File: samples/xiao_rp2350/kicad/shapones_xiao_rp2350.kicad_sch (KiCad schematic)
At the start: 61 parts, among them Q1 PMOS, Q2 NPN, Q3 NPN, SW1 POWER, SW10 MENU, SW2 A, SW3 B, SW4 SELECT, SW5 START, SW6 UP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

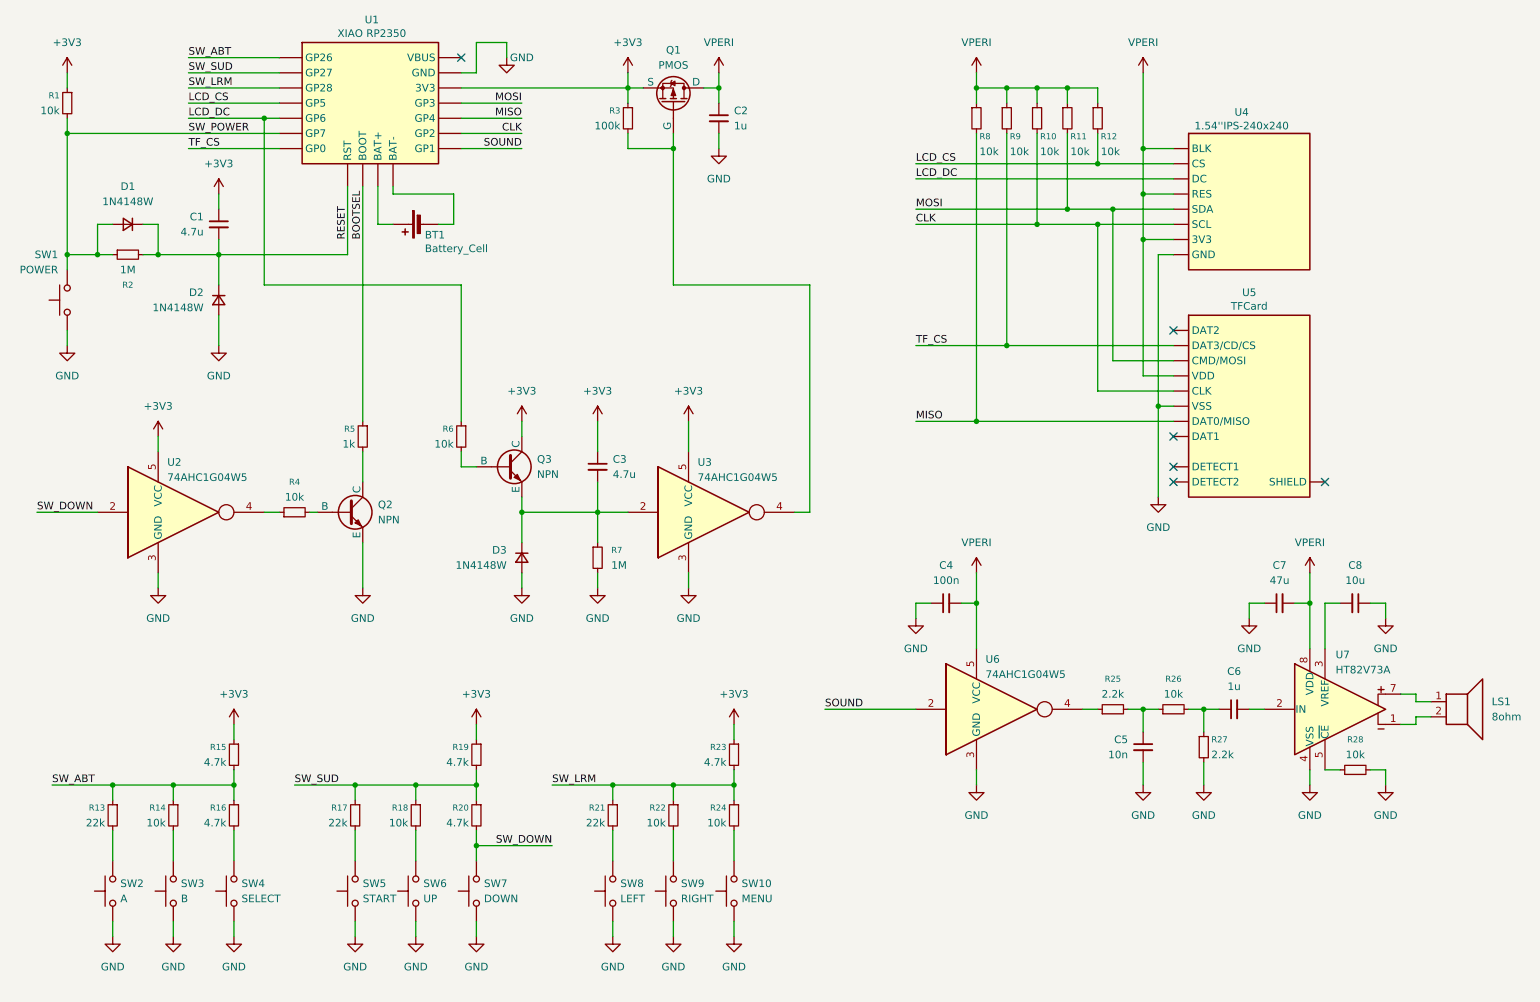
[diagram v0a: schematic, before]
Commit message: add deep sleep function
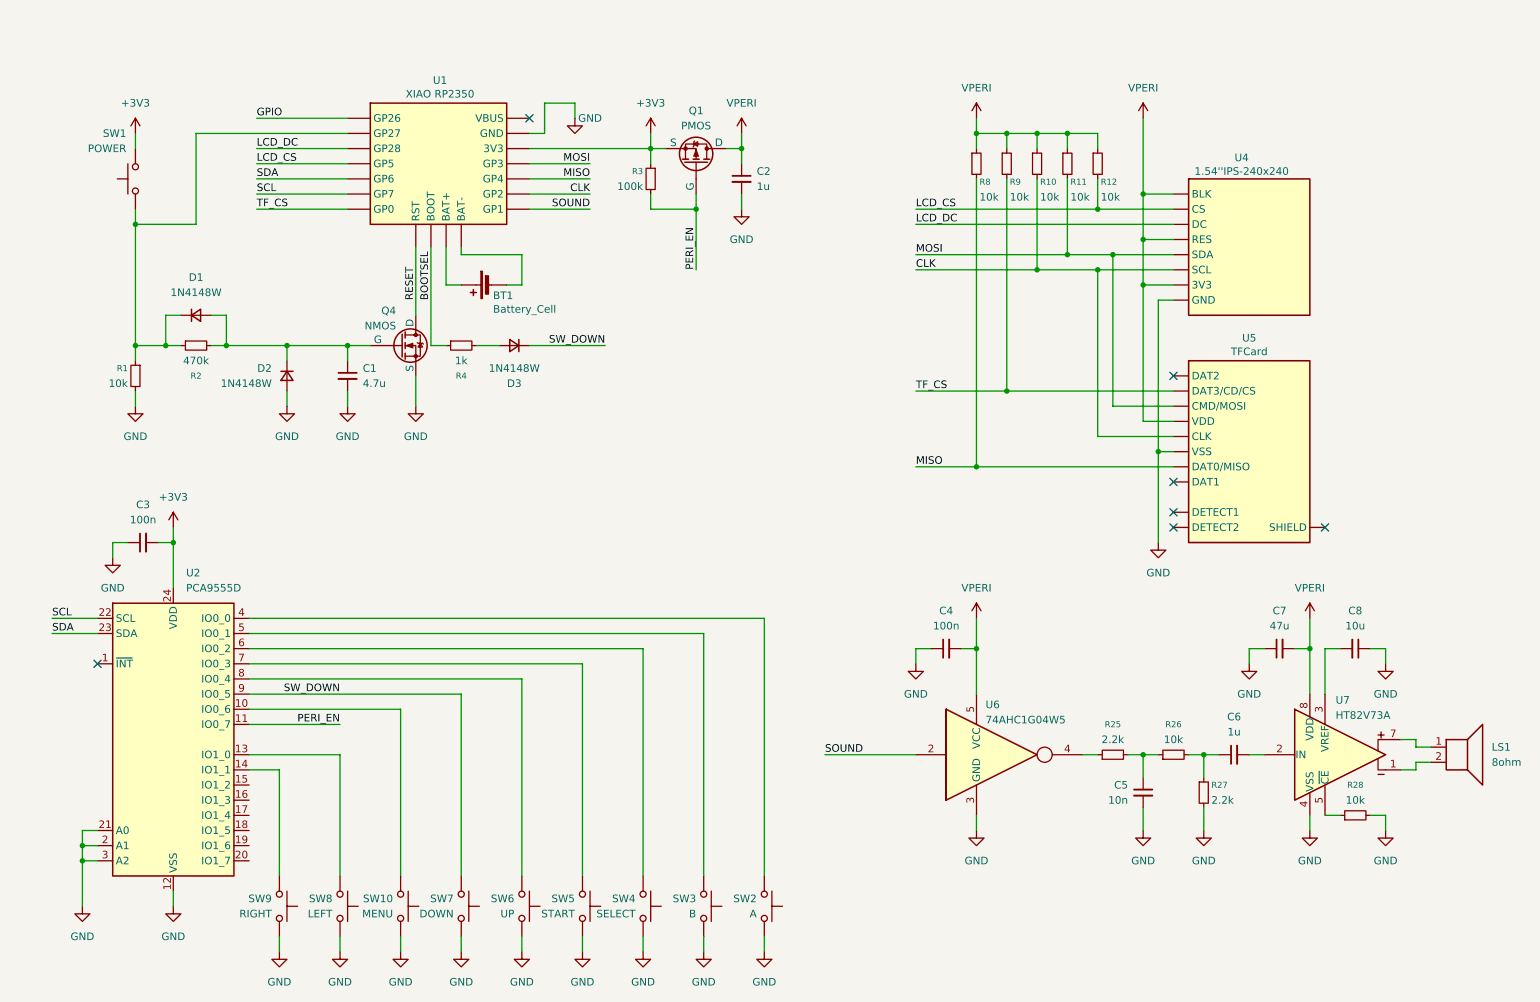
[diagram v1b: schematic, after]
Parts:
- removed Q2, Q3: NPN, symbol Simulation_SPICE:NPN
- removed R13, R17, R21: 22k, symbol Device:R_Small
- removed R14, R18, R22, R24, R6: 10k, symbol Device:R_Small
- removed R15, R16, R19, R20, R23: 4.7k, symbol Device:R_Small
- removed R5: 1k, symbol Device:R_Small
- removed R7: 1M, symbol Device:R_Small
- removed U2, U3: 74AHC1G04W5, Package_TO_SOT_SMD:SOT-553, symbol 74xGxx:74LVC1GU04DRL
- added Q4: NMOS, symbol Simulation_SPICE:NMOS
- added U2: PCA9555D, Package_SO:SOIC-24W_7.5x15.4mm_P1.27mm, symbol Interface_Expansion:PCA9555D
- C3: value 4.7u -> 100n
- R2: value 1M -> 470k
- R4: value 10k -> 1k
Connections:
- net SW_ABT is gone; now on net TF_CS: U1. (GP1)
- net SW_LRM is gone; now on net TF_CS: U1. (GP1)
- net SW_SUD is gone; now on net TF_CS: U1. (GP1)
- net +3V3: now also C3.2, SW1.2, U2.24 (VDD); no longer C1.1, C3.1, R1.1
- net BOOTSEL: now also R4.1
- net GND: now also C1.2, C3.1, R1.2, Q4.3 (S), U2.12 (VSS), U2.2 (A1), U2.21 (A0), U2.3 (A2); no longer D3.2 (A), SW1.1
- net RESET: now also Q4.1 (D); no longer C1.2, D1.1 (K), D2.1 (K), R2.2
- net SW_DOWN: now also D3.1 (K), U2.9 (IO0_5)
- net at SW2.2: now also U2.4 (IO0_0)
- net at SW5.2: now also U2.7 (IO0_3)
- net PERI_EN: now reaches Q1.2 (G), R3.2
- net PERI_EN: now also U2.11 (IO0_7)
- net at SW6.2: now also U2.8 (IO0_4)
- net at R4.2: now also D3.2 (A)
- net at SW9.2: now also U2.14 (IO1_1)
- net at SW3.2: now also U2.5 (IO0_1)
- net at SW8.2: now also U2.13 (IO1_0)
- net at SW10.2: now also U2.10 (IO0_6)
- net at SW4.2: now also U2.6 (IO0_2)
- removed net SW_POWER: D1.2 (A), R1.2, R2.1, SW1.2, U1. (GP1)
- new net: D1.1 (K), R1.1, R2.1, SW1.1, U1. (GP1)
- new net: C1.1, D1.2 (A), D2.1 (K), Q4.2 (G), R2.2
- new net GPIO: U1. (GP1)
- new net SCL: U1. (GP1), U2.22 (SCL)
- new net SDA: U1. (GP1), U2.23 (SDA)
- no-connect marks 6 -> 7
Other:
- moved on the sheet: BT1, C1, C2, C4, C5, C6, C7, C8, D1, D2, LS1, Q1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
